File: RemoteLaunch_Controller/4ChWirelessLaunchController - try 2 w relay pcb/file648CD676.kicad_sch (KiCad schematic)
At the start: 23 parts, among them J1 Pad power and switch, J2 Control board, J3 Pad ch 1, J4 Pad ch 2, J5 Pad ch 3, J6 Pad ch 4, J7 Armed siren, J8 LED/Buzzer Continuity indicat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, J9 LED power indicator, K1 G8N-1U-DC12, K2 Ch 1 relay, K3 G8N-1U-DC12, K4 G8N-1U-DC12, K5 G8N-1U-DC12

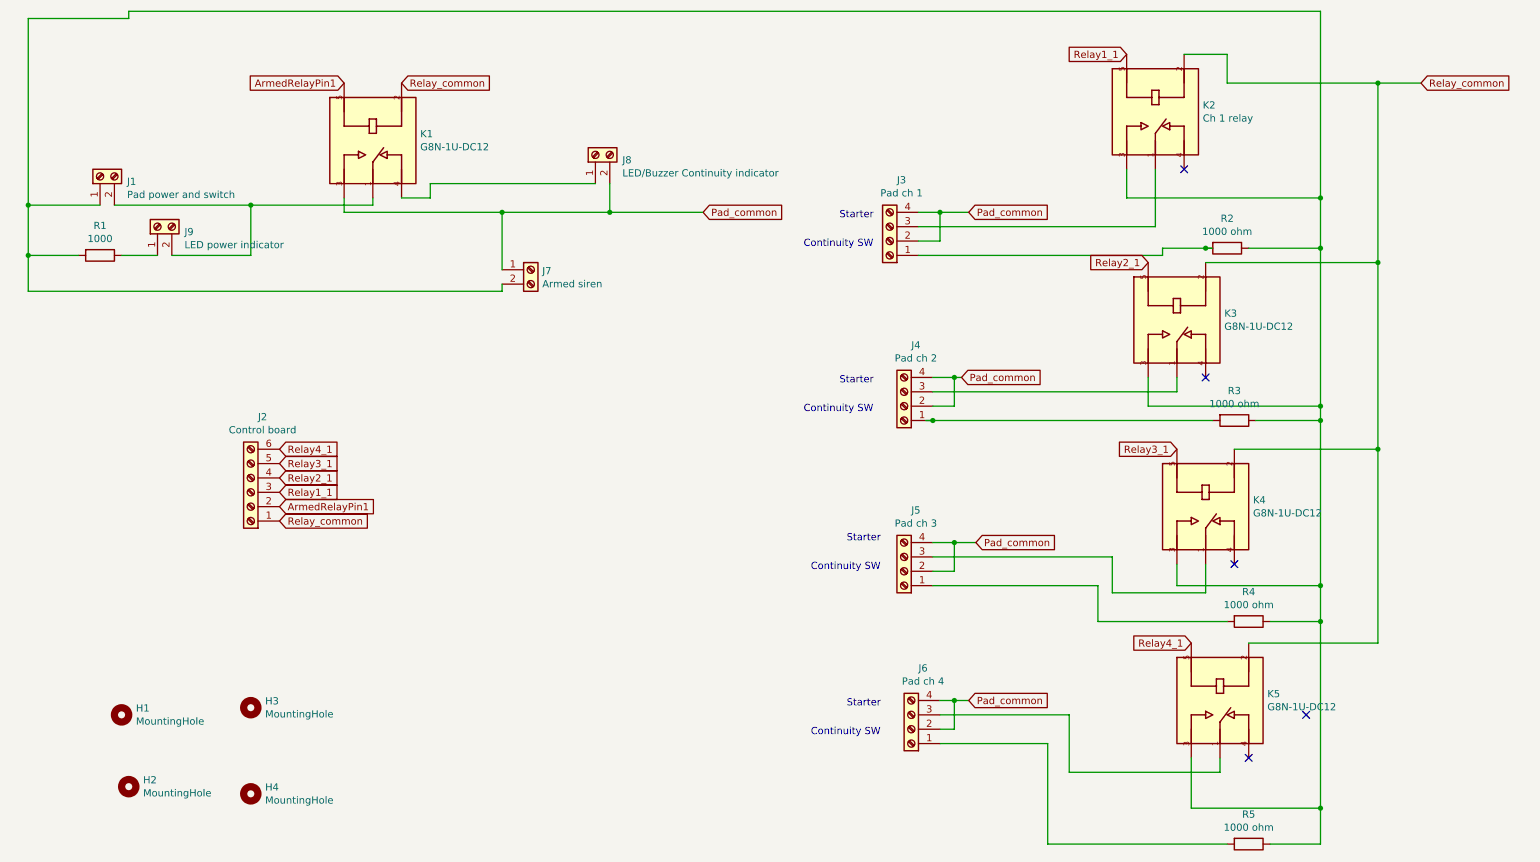
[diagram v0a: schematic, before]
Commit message: Fixing glitch in relay board;  Sending REv4_3 to fab
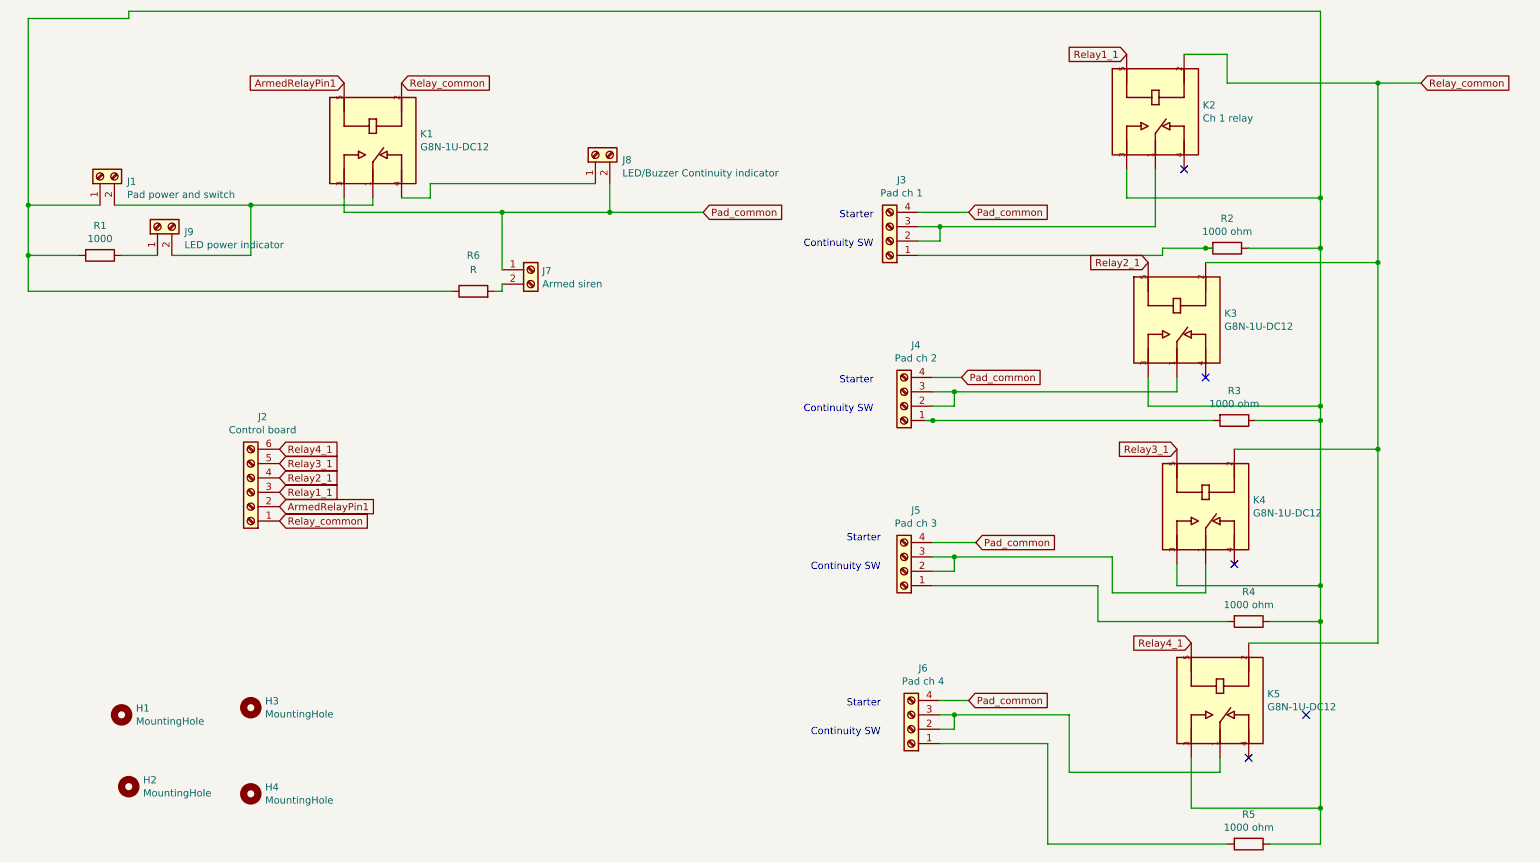
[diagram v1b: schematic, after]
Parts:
- added R6: R, Resistor_THT:R_Axial_DIN0207_L6.3mm_D2.5mm_P7.62mm_Horizontal, symbol Device:R
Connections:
- net Pad_common: no longer J3.2 (Pin_2), J4.2 (Pin_2), J5.2 (Pin_2), J6.2 (Pin_2)
- net at J1.1 (Pin_1), K2.3, K3.3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: now also R6.1; no longer J7.2 (Pin_2)
- net at J3.3 (Pin_3), K2.1: now also J3.2 (Pin_2)
- net at J4.3 (Pin_3), K3.1: now also J4.2 (Pin_2)
- net at J5.3 (Pin_3), K4.1: now also J5.2 (Pin_2)
- net at J6.3 (Pin_3), K5.1: now also J6.2 (Pin_2)
- new net: J7.2 (Pin_2), R6.2
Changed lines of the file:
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@@
 (kicad_sch (version 20230121) (generator eeschema)
   (paper "A4")
-  (junction (at 180.34 81.28) (diameter 0) (color 0 0 0 0)
-  )
-  (junction (at 180.34 110.49) (diameter 0) (color 0 0 0 0)
-  )
   (junction (at 245.11 157.48) (diameter 0) (color 0 0 0 0)
   )
@@
   (junction (at 245.11 86.36) (diameter 0) (color 0 0 0 0)
   )
+  (junction (at 177.8 54.61) (diameter 0) (color 0 0 0 0)
+  )
   (junction (at 16.51 50.8) (diameter 0) (color 0 0 0 0)
   )
   (junction (at 16.51 59.69) (diameter 0) (color 0 0 0 0)
   )
+  (junction (at 180.34 140.97) (diameter 0) (color 0 0 0 0)
+  )
   (junction (at 245.11 58.42) (diameter 0) (color 0 0 0 0)
   )
@@
   (junction (at 119.38 52.07) (diameter 0) (color 0 0 0 0)
   )
-  (junction (at 177.8 52.07) (diameter 0) (color 0 0 0 0)
-  )
   (junction (at 224.79 58.42) (diameter 0) (color 0 0 0 0)
   )
-  (junction (at 180.34 138.43) (diameter 0) (color 0 0 0 0)
+  (junction (at 180.34 113.03) (diameter 0) (color 0 0 0 0)
+  )
+  (junction (at 180.34 83.82) (diameter 0) (color 0 0 0 0)
   )
   (junction (at 176.53 88.9) (diameter 0) (color 0 0 0 0)
@@
     (stroke (width 0) (type default))
   )
-  (wire (pts (xy 180.34 115.57) (xy 180.34 110.49))
+  (wire (pts (xy 177.8 54.61) (xy 215.9 54.61))
     (stroke (width 0) (type default))
   )
@@
     (stroke (width 0) (type default))
   )
-  (wire (pts (xy 177.8 140.97) (xy 200.66 140.97))
+  (wire (pts (xy 177.8 140.97) (xy 180.34 140.97))
     (stroke (width 0) (type default))
   )
@@
     (stroke (width 0) (type default))
   )
-  (wire (pts (xy 176.53 113.03) (xy 208.28 113.03))
+  (wire (pts (xy 176.53 113.03) (xy 180.34 113.03))
     (stroke (width 0) (type default))
   )
@@
     (stroke (width 0) (type default))
   )
-  (wire (pts (xy 173.99 54.61) (xy 215.9 54.61))
-    (stroke (width 0) (type default))
-  )
-  (wire (pts (xy 176.53 83.82) (xy 219.71 83.82))
+  (wire (pts (xy 173.99 54.61) (xy 177.8 54.61))
+    (stroke (width 0) (type default))
+  )
+  (wire (pts (xy 176.53 83.82) (xy 180.34 83.82))
     (stroke (width 0) (type default))
   )
@@
     (stroke (width 0) (type default))
   )
-  (wire (pts (xy 180.34 81.28) (xy 181.61 81.28))
+  (wire (pts (xy 176.53 81.28) (xy 181.61 81.28))
     (stroke (width 0) (type default))
   )
@@
     (stroke (width 0) (type default))
   )
-  (wire (pts (xy 180.34 110.49) (xy 184.15 110.49))
+  (wire (pts (xy 176.53 110.49) (xy 184.15 110.49))
     (stroke (width 0) (type default))
   )
@@
     (stroke (width 0) (type default))
   )
+  (wire (pts (xy 99.06 66.04) (xy 100.33 66.04))
+    (stroke (width 0) (type default))
+  )
   (wire (pts (xy 232.41 128.27) (xy 255.27 128.27))
     (stroke (width 0) (type default))
   )
-  (wire (pts (xy 173.99 52.07) (xy 177.8 52.07))
-    (stroke (width 0) (type default))
-  )
-  (wire (pts (xy 177.8 52.07) (xy 182.88 52.07))
+  (wire (pts (xy 173.99 52.07) (xy 182.88 52.07))
     (stroke (width 0) (type default))
   )
@@
     (stroke (width 0) (type default))
   )
-  (wire (pts (xy 180.34 143.51) (xy 180.34 138.43))
-    (stroke (width 0) (type default))
-  )
   (wire (pts (xy 245.11 86.36) (xy 245.11 88.9))
     (stroke (width 0) (type default))
   )
+  (wire (pts (xy 180.34 113.03) (xy 208.28 113.03))
+    (stroke (width 0) (type default))
+  )
   (wire (pts (xy 255.27 93.98) (xy 255.27 128.27))
     (stroke (width 0) (type default))
@@
     (stroke (width 0) (type default))
   )
+  (wire (pts (xy 177.8 54.61) (xy 177.8 57.15))
+    (stroke (width 0) (type default))
+  )
   (wire (pts (xy 72.39 49.53) (xy 72.39 52.07))
     (stroke (width 0) (type default))
@@
     (stroke (width 0) (type default))
   )
-  (wire (pts (xy 177.8 57.15) (xy 177.8 52.07))
+  (wire (pts (xy 180.34 113.03) (xy 180.34 115.57))
     (stroke (width 0) (type default))
   )
@@
     (stroke (width 0) (type default))
   )
-  (wire (pts (xy 180.34 86.36) (xy 180.34 81.28))
-    (stroke (width 0) (type default))
-  )
   (wire (pts (xy 55.88 50.8) (xy 77.47 50.8))
     (stroke (width 0) (type default))
   )
+  (wire (pts (xy 180.34 140.97) (xy 180.34 143.51))
+    (stroke (width 0) (type default))
+  )
   (wire (pts (xy 34.29 17.78) (xy 34.29 16.51))
     (stroke (width 0) (type default))
@@
     (stroke (width 0) (type default))
   )
+  (wire (pts (xy 180.34 83.82) (xy 219.71 83.82))
+    (stroke (width 0) (type default))
+  )
   (wire (pts (xy 245.11 49.53) (xy 245.11 58.42))
     (stroke (width 0) (type default))
@@
     (stroke (width 0) (type default))
   )
-  (wire (pts (xy 180.34 138.43) (xy 182.88 138.43))
+  (wire (pts (xy 177.8 138.43) (xy 182.88 138.43))
     (stroke (width 0) (type default))
   )
@@
     (stroke (width 0) (type default))
   )
-  (wire (pts (xy 16.51 66.04) (xy 100.33 66.04))
+  (wire (pts (xy 16.51 66.04) (xy 91.44 66.04))
     (stroke (width 0) (type default))
   )
@@
     (stroke (width 0) (type default))
   )
+  (wire (pts (xy 180.34 83.82) (xy 180.34 86.36))
+    (stroke (width 0) (type default))
+  )
   (wire (pts (xy 196.85 163.83) (xy 228.6 163.83))
     (stroke (width 0) (type default))
@@
     (stroke (width 0) (type default))
   )
-  (wire (pts (xy 176.53 81.28) (xy 180.34 81.28))
+  (wire (pts (xy 180.34 140.97) (xy 200.66 140.97))
     (stroke (width 0) (type default))
   )
@@
     (stroke (width 0) (type default))
   )
-  (wire (pts (xy 176.53 110.49) (xy 180.34 110.49))
-    (stroke (width 0) (type default))
-  )
   (wire (pts (xy 31.75 50.8) (xy 55.88 50.8))
-    (stroke (width 0) (type default))
-  )
-  (wire (pts (xy 177.8 138.43) (xy 180.34 138.43))
     (stroke (width 0) (type default))
   )
@@
         )
       )
+    )
+  )
+  (symbol (lib_id "Device:R") (at 95.25 66.04 90) (unit 1)
+    (in_bom yes) (on_board yes) (dnp no) (fields_autoplaced)
+    (property "Reference" "R6" (at 95.25 59.69 90)
+      (effects (font (size 1.27 1.27)))
+    )
+    (property "Value" "R" (at 95.25 62.23 90)
+      (effects (font (size 1.27 1.27)))
+    )
+    (property "Footprint" "Resistor_THT:R_Axial_DIN0207_L6.3mm_D2.5mm_P7.62mm_Horizontal" (at 95.25 67.818 90)
+      (effects (font (size 1.27 1.27)) hide)
+    )
+    (property "Datasheet" "~" (at 95.25 66.04 0)
+      (effects (font (size 1.27 1.27)) hide)
+    )
+    (pin "1")
+    (pin "2")
+    (instances
+      (project "4ChWirelessLaunchController"
+        (path "/eeec8993-d09e-49cb-a9f8-4cbca24d477a/00000000-0000-0000-0000-0000648cd677"
+          (reference "R6") (unit 1)
+        )
+      )

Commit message: latest changes
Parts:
- removed K1: G8N-1U-DC12, CameraTriggerPCB:RELAY_G8N-1U-DC12, symbol 4ChWirelessLaunchController-rescue:G8N-1U-DC12-G8N-1U-DC12
- added K1: G2RL-2-DC24, Relay_THT:Relay_DPDT_Omron_G2RL, symbol Relay:G2RL-2-DC24
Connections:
- net Pad_common: now also K1.5; no longer J7.1 (Pin_1)
- net Relay_common: now also K1.8
- net at J1.2 (Pin_2), J9.2 (Pin_2): now also K1.3, K1.6
- net at J8.1 (Pin_1): now also K1.7
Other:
- moved on the sheet: J1, J2, J7, J8, J9, R1, R6
